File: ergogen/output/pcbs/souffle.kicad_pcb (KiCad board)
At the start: 2 copper layers, 134.9 x 109.8 mm, 162 parts

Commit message: feat: fixed pinout
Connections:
- net MCU1_12 renamed P9
- net MCU1_14 renamed P16
- D26 pad 2: middle_home_B -> mid_home_B
- D55 pad 2: middle_home_F -> mid_home_F
- LED1 pad 2: LED_27 -> LED_35
- LED1 pad 4: LED_26 -> LED_34
- LED10 pad 2: LED_17 -> LED_25
- LED10 pad 4: LED_16 -> LED_24
- LED11 pad 2: LED_16 -> LED_24
- LED11 pad 4: LED_15 -> LED_23
- LED12 pad 2: LED_15 -> LED_23
- LED12 pad 4: LED_14 -> LED_22
- LED13 pad 2: LED_11 -> LED_19
- LED13 pad 4: LED_10 -> LED_18
- LED14 pad 2: LED_12 -> LED_20
- LED14 pad 4: LED_11 -> LED_19
- LED15 pad 2: LED_13 -> LED_21
- LED15 pad 4: LED_12 -> LED_20
- LED16 pad 2: LED_14 -> LED_22
- LED16 pad 4: LED_13 -> LED_21
- LED2 pad 2: LED_26 -> LED_34
- LED2 pad 4: LED_25 -> LED_33
- LED25 pad 2: LED_28 -> LED_18
- LED25 pad 4: LED_27 -> LED_17
- LED26 pad 2: LED_29 -> LED_17
- LED26 pad 4: LED_28 -> LED_16
- LED27 pad 2: LED_31 -> LED_16
- LED27 pad 4: LED_30 -> LED_15
- LED28 pad 2: LED_32 -> LED_15
- LED28 pad 4: LED_31 -> LED_14
- LED29 pad 2: LED_33 -> LED_1
- LED29 pad 4: LED_32 -> ULED_6
- LED3 pad 2: LED_25 -> LED_33
- LED3 pad 4: LED_24 -> LED_32
- LED4 pad 2: LED_24 -> LED_32
- LED4 pad 4: LED_23 -> LED_31
- LED5 pad 2: LED_19 -> LED_27
- LED5 pad 4: LED_18 -> LED_26
- LED6 pad 2: LED_20 -> LED_28
- LED6 pad 4: LED_21 -> LED_27
- LED7 pad 2: LED_21 -> LED_29
- LED7 pad 4: LED_22 -> LED_28
- LED8 pad 2: LED_22 -> LED_30
- LED8 pad 4: LED_23 -> LED_29
- LED9 pad 2: LED_18 -> LED_26
- LED9 pad 4: LED_17 -> LED_25
- MCU1 pad 10: MCU1_10 -> R2
- MCU1 pad 11: MCU1_11 -> R3
- MCU1 pad 13: MCU1_13 -> P10
- MCU1 pad 15: MCU1_15 -> C5
- MCU1 pad 16: MCU1_16 -> C4
- MCU1 pad 17: MCU1_17 -> C3
- MCU1 pad 18: MCU1_18 -> C2
- MCU1 pad 19: MCU1_19 -> C1
- MCU1 pad 20: MCU1_20 -> C0
- MCU1 pad 5: MCU1_5 -> SDA
- MCU1 pad 6: MCU1_6 -> SCL
- MCU1 pad 7: MCU1_7 -> CS
- MCU1 pad 8: MCU1_8 -> R0
- MCU1 pad 9: MCU1_9 -> R1
- S26 pad 1: middle_home_B -> mid_home_B
- S55 pad 1: middle_home_F -> mid_home_F
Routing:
- net (no net): track 333.1 -> 111.0 mm
- net LED_34: track 0.00 -> 13.5 mm, vias 0 -> 2
- net LED_13: track 13.5 -> 0.00 mm, vias 2 -> 0
- net LED_12: track 13.5 -> 0.00 mm, vias 2 -> 0
- net LED_11: track 13.5 -> 0.00 mm, vias 2 -> 0
- net LED_33: track 6.76 -> 13.5 mm, vias 1 -> 2
- net LED_14: track 13.5 -> 6.76 mm, vias 2 -> 1
- net LED_35: track 0.00 -> 6.76 mm, vias 0 -> 1
- net LED_29: track 6.76 -> 13.5 mm, vias 1 -> 2
- net LED_20: track 6.76 -> 13.5 mm, vias 1 -> 2
- net LED_19: track 6.76 -> 13.5 mm, vias 1 -> 2
- net LED_10: track 13.5 -> 6.76 mm, vias 2 -> 1
- net LED_31: track 13.5 -> 6.76 mm, vias 2 -> 1
- net ULED_6: track 6.76 -> 13.5 mm, vias 1 -> 2
- net LED_1: track 6.76 -> 13.5 mm, vias 1 -> 2

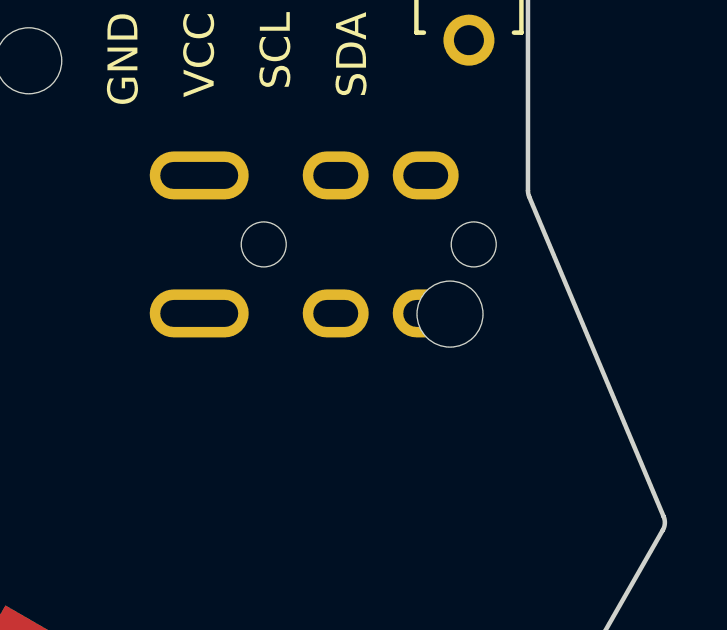
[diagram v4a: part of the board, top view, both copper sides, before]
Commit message: feat: adjusted the screw hole instead
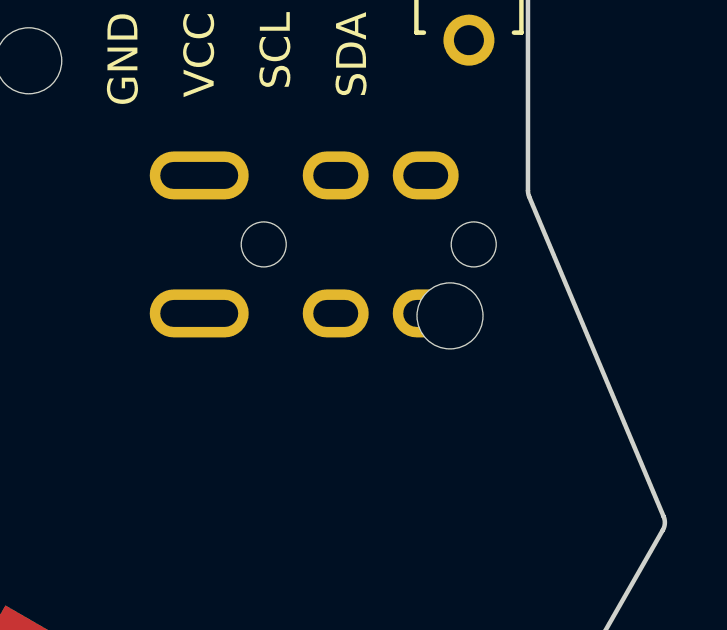
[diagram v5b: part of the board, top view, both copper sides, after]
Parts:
- moved MH2 0.06 mm to (219.0, 108.9)
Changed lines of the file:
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@@
   (footprint "ceoloide:mounting_hole_npth"
     (layer "F.Cu")
-    (at 218.969 108.8825 0)
+    (at 218.969 108.9425 0)
     (property "Reference" "MH2"
       (at 0 2.55 0)
